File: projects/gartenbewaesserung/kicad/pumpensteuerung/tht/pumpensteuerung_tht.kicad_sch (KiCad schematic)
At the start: 7 parts, among them J2 Screw_Terminal_01x02, J3 I2C Terminal

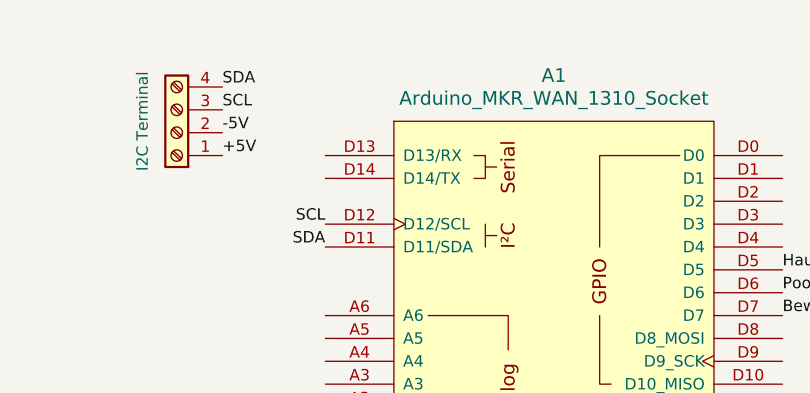
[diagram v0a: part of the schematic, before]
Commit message: [gartenbewaesserung(pcb)] replace fake footprints with real one
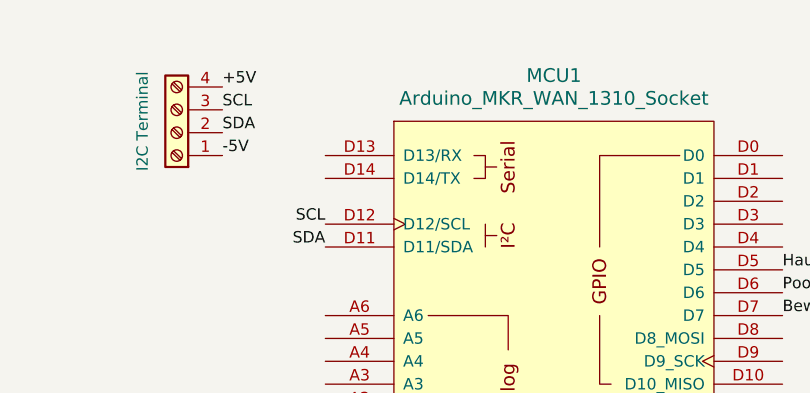
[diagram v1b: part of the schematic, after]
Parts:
- J2: footprint TerminalBlock:TerminalBlock_Altech_AK300-2_P5.00mm -> PhoenixContact:MKDSN 1,5_2-5,08
- J3: footprint TerminalBlock:TerminalBlock_Altech_AK300-4_P5.00mm -> PhoenixContact:MKDSN 1,5_4-5,08
- renumbered A1 to MCU1
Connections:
- net +5V: now also J3.4 (Pin_4); no longer J3.1 (Pin_1)
- net -5V: now also J3.1 (Pin_1); no longer J3.2 (Pin_2)
- net SDA: now also J3.2 (Pin_2); no longer J3.4 (Pin_4)
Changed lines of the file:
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@@
 	)
 	(label "-5V"
-		(at 83.82 24.13 0)
+		(at 83.82 26.67 0)
 		(effects
 			(font
@@
 	)
 	(label "+5V"
-		(at 83.82 26.67 0)
+		(at 83.82 19.05 0)
 		(effects
 			(font
@@
 	)
 	(label "SDA"
-		(at 83.82 19.05 0)
+		(at 83.82 24.13 0)
 		(effects
 			(font
@@
 		(dnp no)
 		(fields_autoplaced yes)
-		(property "Reference" "A1"
+		(property "Reference" "MCU1"
 			(at 120.65 17.78 0)
 			(effects
@@
 			(project ""
 				(path "/21a07dfa-371b-4773-840e-44a8dfeac208"
-					(reference "A1")
+					(reference "MCU1")
 					(unit 1)
 				)
@@
 			)
 		)
-		(property "Footprint" "TerminalBlock:TerminalBlock_Altech_AK300-4_P5.00mm"
+		(property "Footprint" "PhoenixContact:MKDSN 1,5_4-5,08"
 			(at 78.74 24.13 0)
 			(effects
@@
 			)
 		)
-		(property "Footprint" "TerminalBlock:TerminalBlock_Altech_AK300-2_P5.00mm"
+		(property "Footprint" "PhoenixContact:MKDSN 1,5_2-5,08"
 			(at 29.21 63.5 0)
 			(effects
